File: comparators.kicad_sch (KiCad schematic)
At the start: 77 parts, among them SW7 SW_DIP_x03, U41 TLV3502AIDR, U42 TLV3502AIDR, U43 TLV3502AIDR, U44 TLV3502AIDR, U45 TLV3502AIDR, U46 TLV3502AIDR, U47 TLV3502AIDR, U48 TLV3502AIDR, U49 TLV3502AIDR, U50 TLV3502AIDR, U51 TLV3502AIDR, U52 TLV3502AIDR, U53 TXB0108PW, U54 TXB0108PW, U55 TXB0108PW

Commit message: series resistors
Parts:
- added C128, C129, C130, C131, C132, C133: 100n, symbol Device:C
- added C134: 1u, symbol Device:C
- added R66, R67, R68, R69, R70, R71, R72, R73, R74, R75, R76, R77, R78, R79, R80, R81, R82, R83, R84, R85, R86, R87, R88, R89: 10R, symbol Device:R
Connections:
- net +3V3: now also C131.1, C132.1, C133.1
- net COMP_VCC: now also C128.1, C129.1, C130.1, C134.1
- net GND: now also C128.2, C129.2, C130.2, C131.2, C132.2, C133.2, C134.2
- net OUT0: now also R66.1; no longer U53.20 (B1)
- net OUT1: now also R67.1; no longer U53.18 (B2)
- net OUT10: now also R76.1; no longer U54.17 (B3)
- net OUT11: now also R77.1; no longer U54.16 (B4)
- net OUT12: now also R78.1; no longer U54.15 (B5)
- net OUT13: now also R79.1; no longer U54.14 (B6)
- net OUT14: now also R80.1; no longer U54.13 (B7)
- net OUT15: now also R81.1; no longer U54.12 (B8)
- net OUT16: now also R82.1; no longer U55.20 (B1)
- net OUT17: now also R83.1; no longer U55.18 (B2)
- net OUT18: now also R84.1; no longer U55.17 (B3)
- net OUT19: now also R85.1; no longer U55.16 (B4)
- net OUT2: now also R68.1; no longer U53.17 (B3)
- net OUT20: now also R86.1; no longer U55.15 (B5)
- net OUT21: now also R87.1; no longer U55.14 (B6)
- net OUT22: now also R88.1; no longer U55.13 (B7)
- net OUT23: now also R89.1; no longer U55.12 (B8)
- net OUT3: now also R69.1; no longer U53.16 (B4)
- net OUT4: now also R70.1; no longer U53.15 (B5)
- net OUT5: now also R71.1; no longer U53.14 (B6)
- net OUT6: now also R72.1; no longer U53.13 (B7)
- net OUT7: now also R73.1; no longer U53.12 (B8)
- net OUT8: now also R74.1; no longer U54.20 (B1)
- net OUT9: now also R75.1; no longer U54.18 (B2)
- new net: R67.2, U53.18 (B2)
- new net: R81.2, U54.12 (B8)
- new net: R80.2, U54.13 (B7)
- new net: R79.2, U54.14 (B6)
- new net: R78.2, U54.15 (B5)
- new net: R77.2, U54.16 (B4)
- new net: R76.2, U54.17 (B3)
- new net: R75.2, U54.18 (B2)
- new net: R74.2, U54.20 (B1)
- new net: R73.2, U53.12 (B8)
- new net: R72.2, U53.13 (B7)
- new net: R71.2, U53.14 (B6)
- new net: R70.2, U53.15 (B5)
- new net: R69.2, U53.16 (B4)
- new net: R68.2, U53.17 (B3)
- new net: R66.2, U53.20 (B1)
- new net: R85.2, U55.16 (B4)
- new net: R88.2, U55.13 (B7)
- new net: R83.2, U55.18 (B2)
- new net: R89.2, U55.12 (B8)
- new net: R87.2, U55.14 (B6)
- new net: R86.2, U55.15 (B5)
- new net: R84.2, U55.17 (B3)
- new net: R82.2, U55.20 (B1)
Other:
- moved on the sheet: SW7, TP12, U53, U54, U55

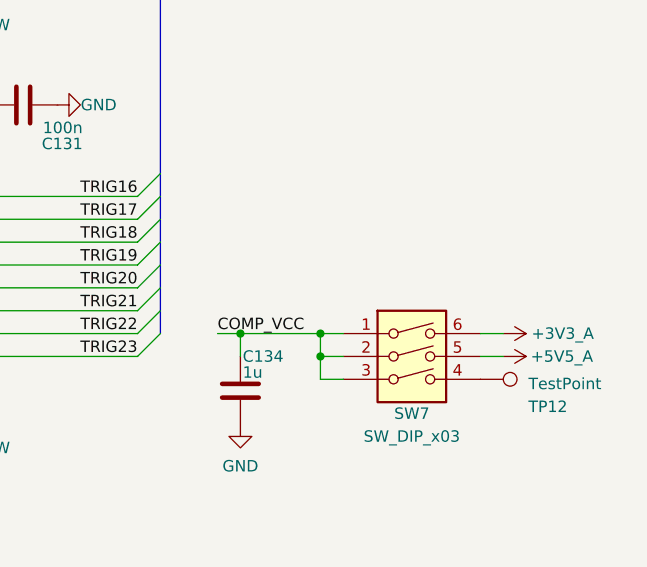
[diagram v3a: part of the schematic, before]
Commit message: annotate dip switches
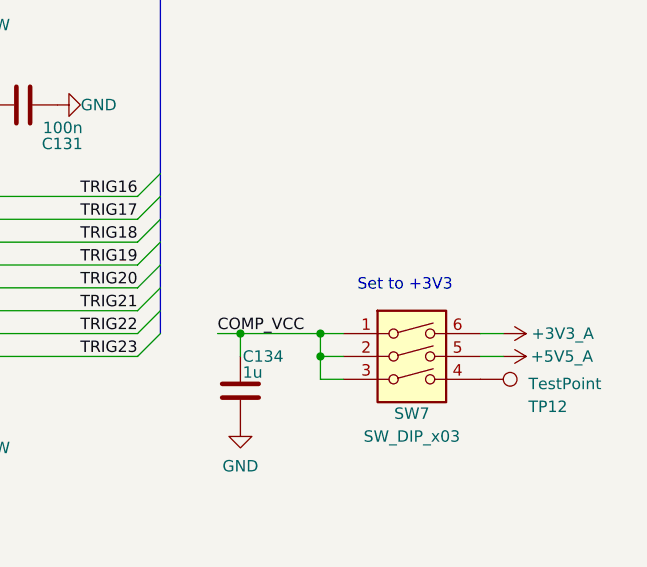
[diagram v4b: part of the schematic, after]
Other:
- note added: "Set to +3V3"
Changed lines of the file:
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@@
 	(generator_version "9.0")
 	(paper "A4")
+	(text "Set to +3V3"
+		(exclude_from_sim no)
+		(at 259.588 139.446 0)
+		(effects
+			(font
+				(size 1.27 1.27)
+			)
+		)
+	)
 	(junction
 		(at 41.91 39.37)
